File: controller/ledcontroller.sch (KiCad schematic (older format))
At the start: 57 parts, among them J1 USB_A, J2 Pulse-J0026D21B, J3 STELVIO-2P-508, J4 STELVIO-2P-508, J5 STELVIO-5P-508, J6 STELVIO-4P-508, P1 FDI_Cable, P2 CONN_01X02, P3 CONN_01X02, P4 CONN_01X02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

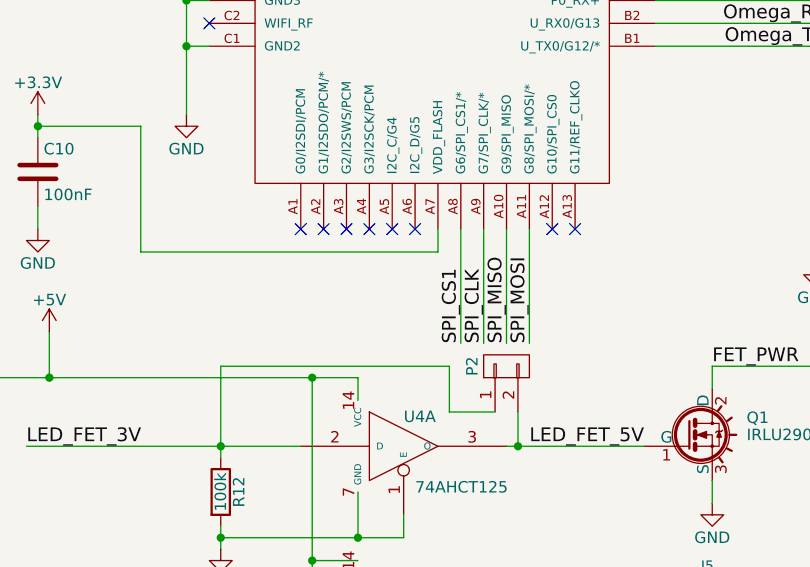
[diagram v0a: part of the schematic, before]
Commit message: Move MCP3002 SPI to GPIO 0..3 pins of Omega2 (HW SPI does not work)
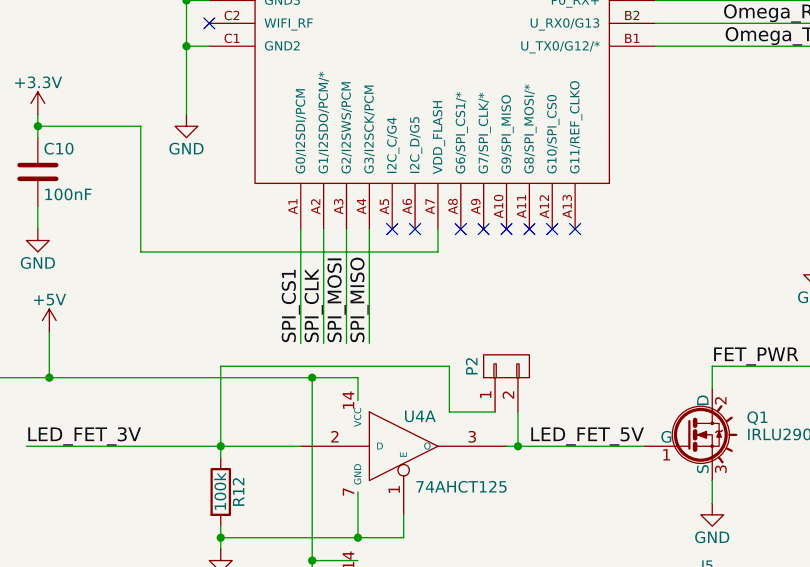
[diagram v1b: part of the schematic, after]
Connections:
- net SPI_CLK: now also U1.A2 (G1/I2SDO/PCM/*); no longer U1.A9 (G7/SPI_CLK/*)
- net SPI_CS1: now also U1.A1 (G0/I2SDI/PCM); no longer U1.A8 (G6/SPI_CS1/*)
- net SPI_MISO: now also U1.A4 (G3/I2SCK/PCM); no longer U1.A10 (G9/SPI_MISO)
- net SPI_MOSI: now also U1.A3 (G2/I2SWS/PCM); no longer U1.A11 (G8/SPI_MOSI/*)
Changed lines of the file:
@@
 NoConn ~ 6250 4050
 NoConn ~ 6350 4050
-NoConn ~ 5150 4050
-NoConn ~ 5250 4050
-NoConn ~ 5350 4050
-NoConn ~ 5450 4050
 Text Label 7250 950  2    60   ~ 0
 USB-
@@
 Wire Wire Line
 	5750 4150 5750 4050
-Wire Wire Line
-	5850 4050 5850 4550
-Wire Wire Line
-	5950 4050 5950 4550
-Wire Wire Line
-	6050 4050 6050 4550
-Wire Wire Line
-	6150 4050 6150 4550
-Text Label 5850 4550 1    60   ~ 0
+Text Label 5150 4550 1    60   ~ 0
 SPI_CS1
-Text Label 5950 4550 1    60   ~ 0
+Text Label 5250 4550 1    60   ~ 0
 SPI_CLK
-Text Label 6050 4550 1    60   ~ 0
+Text Label 5450 4550 1    60   ~ 0
 SPI_MISO
-Text Label 6150 4550 1    60   ~ 0
+Text Label 5350 4550 1    60   ~ 0
 SPI_MOSI
 Wire Wire Line
@@
 Text Label 3350 6350 0    60   ~ 0
 SENS_PWR
+Wire Wire Line
+	5150 4050 5150 4550
+Wire Wire Line
+	5250 4050 5250 4550
+Wire Wire Line
+	5350 4050 5350 4550
+Wire Wire Line
+	5450 4050 5450 4550
+NoConn ~ 5850 4050
+NoConn ~ 5950 4050
+NoConn ~ 6050 4050
+NoConn ~ 6150 4050
 $EndSCHEMATC

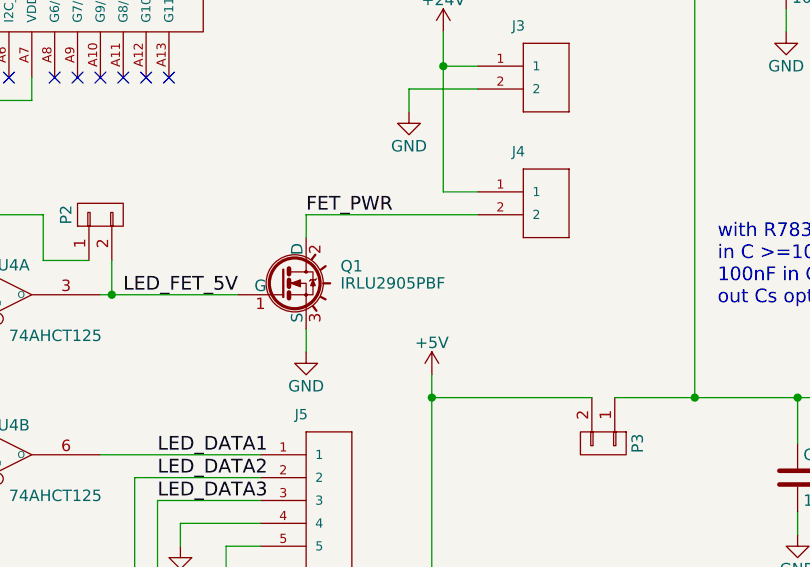
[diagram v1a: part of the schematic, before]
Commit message: Schematics: Q1 is SMT, we had the THT variant (IRLU vs IRLR)
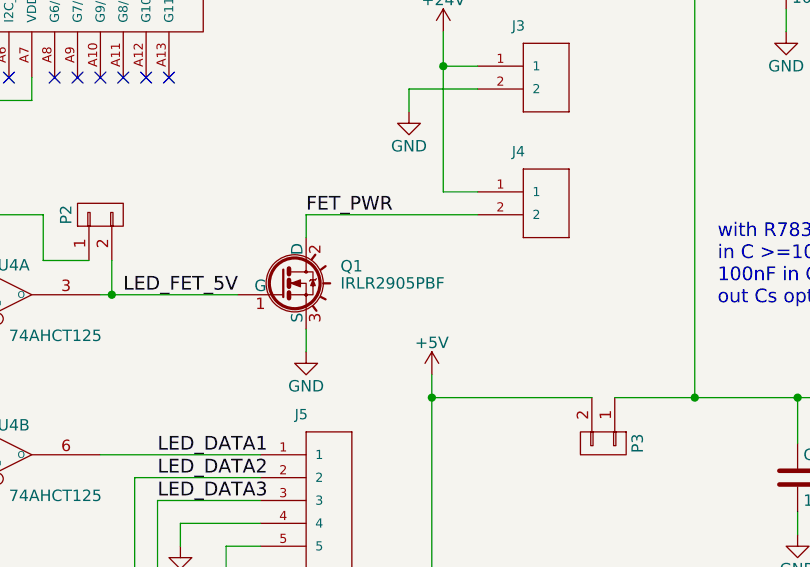
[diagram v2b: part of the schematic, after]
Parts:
- Q1: value IRLU2905PBF -> IRLR2905PBF; Field4 (none) -> distrelec.ch; Field5 (none) -> 171-18-672
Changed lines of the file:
@@
 P 6850 4950
 F 0 "Q1" H 7100 5025 50  0000 L CNN
-F 1 "IRLU2905PBF" H 7100 4950 50  0000 L CNN
+F 1 "IRLR2905PBF" H 7100 4950 50  0000 L CNN
 F 2 "TO_SOT_Packages_SMD:TO-252-2" H 7100 4875 50  0001 L CIN
 F 3 "" H 6850 4950 50  0001 L CNN
+F 4 "distrelec.ch" H 6850 4950 60  0001 C CNN "Field4"
+F 5 "171-18-672" H 6850 4950 60  0001 C CNN "Field5"
 	1    6850 4950
 	1    0    0    -1

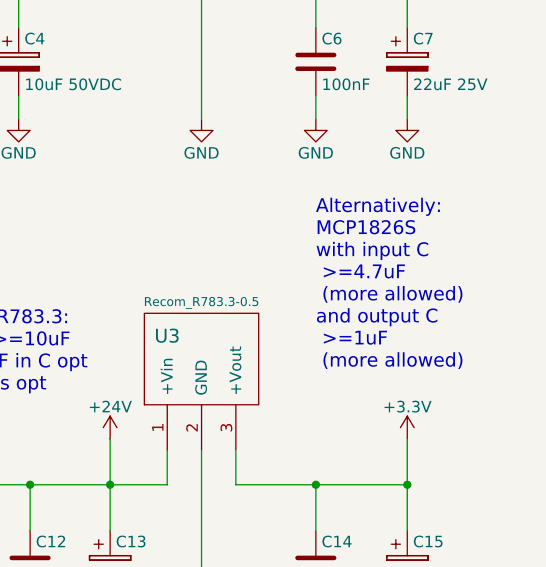
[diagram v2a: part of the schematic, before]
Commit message: Schematics: MCP1826S is deprecated, using LM3940IT instead, different (more difficult) specs for required capacitors
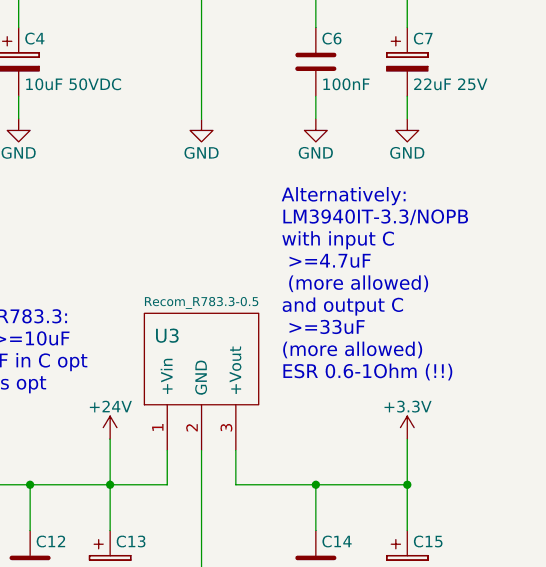
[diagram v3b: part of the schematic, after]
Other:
- note added: "Alternatively:\nLM3940IT-3.3/NOPB\nwith input C\n >=4.7uF\n (more allowed)\nand output C\n >=33uF\n(more allowed)\nESR 0.6-1Ohm (!!)"
- note removed: "Alternatively:\nMCP1826S\nwith input C\n >=4.7uF\n (more allowed)\nand output C\n >=1uF\n (more allowed)"
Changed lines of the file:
@@
 	1    0    0    -1
 $EndComp
-Text Notes 10350 4950 0    60   ~ 0
-Alternatively:\nMCP1826S\nwith input C\n >=4.7uF\n (more allowed)\nand output C\n >=1uF\n (more allowed)
+Text Notes 10200 5000 0    60   ~ 0
+Alternatively:\nLM3940IT-3.3/NOPB\nwith input C\n >=4.7uF\n (more allowed)\nand output C\n >=33uF\n(more allowed)\nESR 0.6-1Ohm (!!)
 Text Notes 8750 5050 0    60   ~ 0
 with R783.3:\nin C >=10uF\n100nF in C opt\nout Cs opt

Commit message: ledcontroller v2: connector holes, better power selection, FET driver, silk info
- use updated connectors from plan44 library with larger holes (and correct reference points)

- separated 5V and 24V such that 24V FET can be used even if we also have 5V

- swapped PWM2+3 output lines to match connector signal name/order.

- pulldown for FET driver changed to 10k (100k was apparently too weak)

- pinout info for connectors on silk screen
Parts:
- added P6, P7: CONN_01X02, plan44:CONFIG-PAD-2P, symbol CONN_01X02
- R12: value 100k -> 10k
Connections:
- net +24V: now also P6.2 (P2); no longer C12.1, C13.1, C4.1, P3.1 (P1), U2.1 (+Vin), U3.1 (+Vin)
- net LED_DATA2_3V: now also U1.B13 (U_TX2/G20/PWM2/P2_TX+); no longer U1.B14 (U_RX2/G21/PWM3/P2_TX-)
- net LED_DATA3_3V: now also U1.B14 (U_RX2/G21/PWM3/P2_TX-); no longer U1.B13 (U_TX2/G20/PWM2/P2_TX+)
- net LED_FET_5V: now also P7.1 (P1); no longer U4.3 (O)
- new net: P7.2 (P2), U4.3 (O)
- new net V_REG_IN: C12.1, C13.1, C4.1, P3.1 (P1), P6.1 (P1), U2.1 (+Vin), U3.1 (+Vin)
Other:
- moved on the sheet: J3, J4, P2
